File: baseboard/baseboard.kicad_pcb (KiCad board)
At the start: 2 copper layers, 99.8 x 99.8 mm, 36 parts, among them IC1 ATA6561-GAQW-N, J11 Conn_01x02_Pin, J13 Conn_02x05_Odd_Even, J14 Conn_02x25_Odd_Even, J6 Screw_Terminal_01x02, J7 Conn_02x25_Odd_Even, J8 Conn_01x02_Pin, U1 PY32E407V1xT_START

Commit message: artwork confirm
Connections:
- J14 pad 19: /WIPER -> /F2
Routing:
- net /Pmod3_2: track 43.6 -> 79.8 mm
- net /WIPER: track 8.44 -> 0.00 mm
- net /F2: track 0.00 -> 8.44 mm
- net /ETH_RMII_TXD1: track 26.5 -> 24.2 mm
- net /Pmod2_4: track 78.8 -> 80.9 mm
- net +3V3: track 423.5 -> 422.4 mm
- net /Pmod3_1: track 48.8 -> 49.5 mm
- net /Pmod2_3: track 43.5 -> 44.1 mm
- net GND: vias 84 -> 89
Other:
- board size 99.8 x 99.8 mm -> 99.8 x 93.2 mm
- board text added: "5V"
- board text added: "A3"
- board text added: "A4"
- board text added: "A5"
- board text added: "A6"
- board text added: "B12|B11"
- board text added: "B2|E13"
- board text added: "C10|A11"
- board text added: "C12|A10"
- board text added: "C6"
- board text added: "C7"
- board text added: "D10|D9"
- board text added: "D13"
- board text added: "D14"
- board text added: "D2|F4"
- board text added: "D3|D7"
- board text added: "D4|C9"
- board text added: "D5|B6"
- board text added: "D6|C8"
- board text added: "D8|A1"
- board text added: "E0|E5"
- board text added: "E15|D15"
- board text added: "E1|E6"
- board text added: "E2|E4"
- board text added: "E3|E14"
- board text added: "E7|E12"
- board text added: "E8|E11"
- board text added: "E9|E10"
- board text added: "G"
- board text added: "H L"
- board text added: "NC|A2"
- board text added: "NC|B13"
- board text added: "NC|C1"
- board text added: "NRST"
- board text added: "Pmod EXP v0.1 for PY32E407-START-ETH V2.1"
- board text added: "RXD"
- board text added: "TXD"
- board text added: "V"

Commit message: plot
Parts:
- moved J6 5.08 mm to (117.3, 83.7), turned to 180 degrees
- moved D5 0.25 mm to (114.8, 80.0)
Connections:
- D5 pad 1: Net-(J6-Pin_2) -> Net-(J6-Pin_1)
- J6 pad 1: Net-(J11-Pin_2) -> Net-(J6-Pin_1)
- J6 pad 2: Net-(J6-Pin_2) -> Net-(J11-Pin_2)
- J8 pad 1: Net-(J6-Pin_2) -> Net-(J6-Pin_1)
- L1 pad 2: Net-(J6-Pin_2) -> Net-(J6-Pin_1)
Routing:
- net Net-(J6-Pin_2): track 27.1 -> 0.00 mm
- net Net-(J6-Pin_1): track 0.00 -> 27.1 mm
- net +3V3: track 422.4 -> 434.1 mm
- net GND: track 40.4 -> 49.9 mm, vias 89 -> 92
- net Net-(J8-Pin_2): track 3.16 -> 2.65 mm
- net Net-(J11-Pin_1): track 3.15 -> 2.64 mm
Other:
- board text added: "3V3"
- board text added: "G|3V3"
- board text added: "JTCK"
- board text added: "JTDI"
- board text added: "JTDO"
- board text added: "JTMS"
- board text added: "NC"
- board text added: "VREF|VSSA"

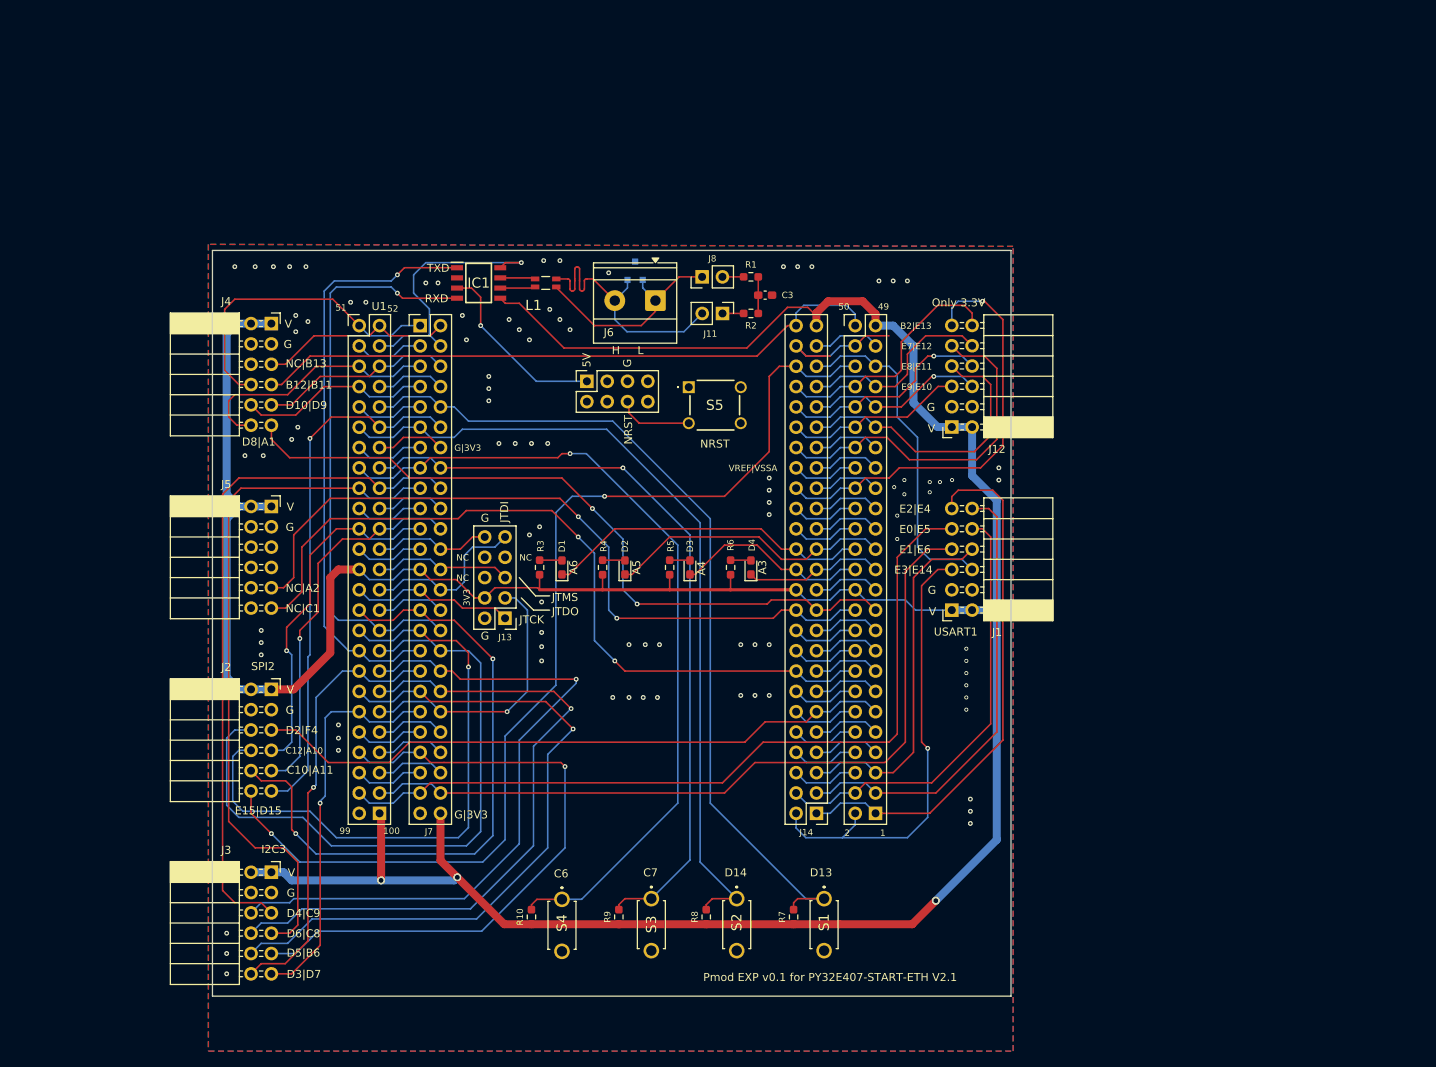
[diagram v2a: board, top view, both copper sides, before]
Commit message: add t1s on baseboard
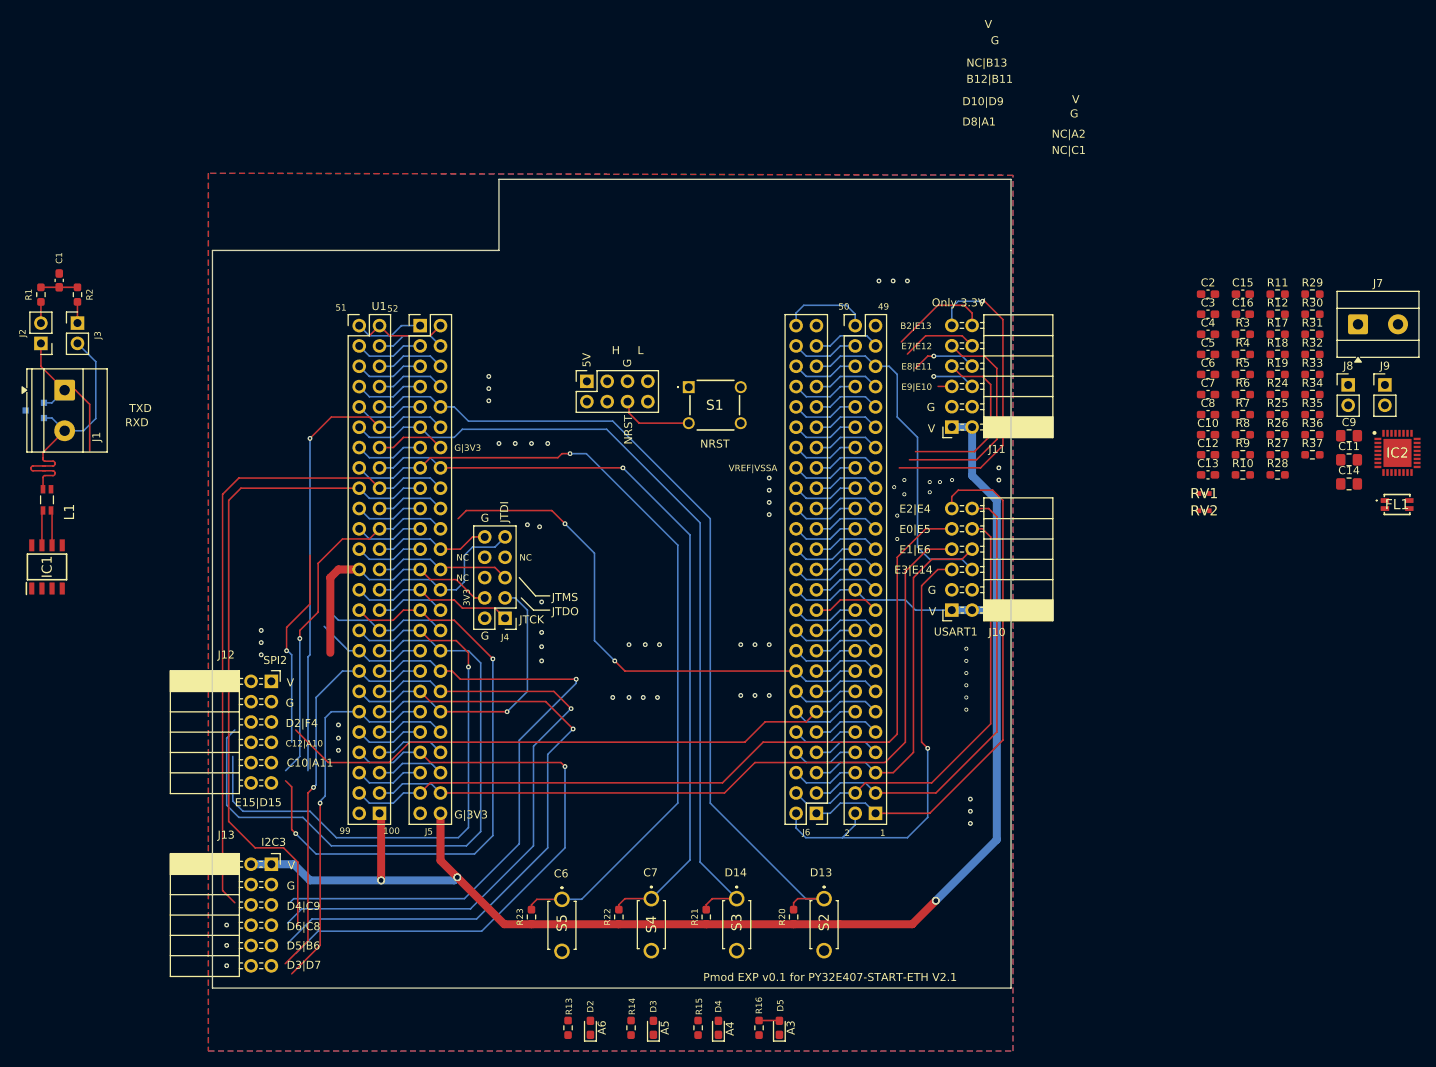
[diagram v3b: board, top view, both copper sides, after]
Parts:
- removed the J4 at (69.3, 86.6)
- removed the J5 at (69.3, 109.5)
- added C10: 0.1u, Capacitor_SMD:C_0603_1608Metric_Pad1.08x0.95mm_HandSolder, F.Cu at (186.4, 100.5)
- added C11: 10u, Capacitor_SMD:C_0805_2012Metric_Pad1.18x1.45mm_HandSolder, F.Cu at (204.1, 103.6)
- added C12: 10000p, Capacitor_SMD:C_0603_1608Metric_Pad1.08x0.95mm_HandSolder, F.Cu at (186.4, 103.0)
- added C13: 0.1u, Capacitor_SMD:C_0603_1608Metric_Pad1.08x0.95mm_HandSolder, F.Cu at (186.4, 105.5)
- added C14: 10u, Capacitor_SMD:C_0805_2012Metric_Pad1.18x1.45mm_HandSolder, F.Cu at (204.1, 106.7)
- added C15: 10000p, Capacitor_SMD:C_0603_1608Metric_Pad1.08x0.95mm_HandSolder, F.Cu at (190.8, 82.9)
- added C16: 0.1u, Capacitor_SMD:C_0603_1608Metric_Pad1.08x0.95mm_HandSolder, F.Cu at (190.8, 85.4)
- added C2: 0.22u, Capacitor_SMD:C_0603_1608Metric_Pad1.08x0.95mm_HandSolder, F.Cu at (186.4, 82.9)
- added C3: 0.22u, Capacitor_SMD:C_0603_1608Metric_Pad1.08x0.95mm_HandSolder, F.Cu at (186.4, 85.4)
- added C4: 0.1u, Capacitor_SMD:C_0603_1608Metric_Pad1.08x0.95mm_HandSolder, F.Cu at (186.4, 88.0)
- added C5: 0.1u, Capacitor_SMD:C_0603_1608Metric_Pad1.08x0.95mm_HandSolder, F.Cu at (186.4, 90.5)
- added C6: 10000p, Capacitor_SMD:C_0603_1608Metric_Pad1.08x0.95mm_HandSolder, F.Cu at (186.4, 93.0)
- added C7: 0.1u, Capacitor_SMD:C_0603_1608Metric_Pad1.08x0.95mm_HandSolder, F.Cu at (186.4, 95.5)
- added C8: 10000p, Capacitor_SMD:C_0603_1608Metric_Pad1.08x0.95mm_HandSolder, F.Cu at (186.4, 98.0)
- added C9: 10u, Capacitor_SMD:C_0805_2012Metric_Pad1.18x1.45mm_HandSolder, F.Cu at (204.1, 100.6)
- added FL1: ACT1210E-131-2P-TL00, kicad9_samacsys:ACT1210E1312PTL00, F.Cu at (210.1, 109.2)
- added IC2: LAN8670C2-E_LMX, kicad9_samacsys:QFN50P500X500X100-33N-D, F.Cu at (210.1, 102.8)
- added J7: Screw_Terminal_01x02, TerminalBlock_MetzConnect:TerminalBlock_MetzConnect_Type055_RT01502HDWU_1x02_P5.00mm_Horizontal, F.Cu at (205.2, 86.7)
- added J8: Conn_01x02_Pin, Connector_PinHeader_2.54mm:PinHeader_1x02_P2.54mm_Vertical, F.Cu at (203.9, 94.3)
- added J9: Conn_01x02_Pin, Connector_PinHeader_2.54mm:PinHeader_1x02_P2.54mm_Vertical, F.Cu at (208.5, 94.3)
- added R10: 10k, Resistor_SMD:R_0603_1608Metric_Pad0.98x0.95mm_HandSolder, F.Cu at (190.8, 105.5)
- added R11: 10k, Resistor_SMD:R_0603_1608Metric_Pad0.98x0.95mm_HandSolder, F.Cu at (195.1, 82.9)
- added R12: 10k, Resistor_SMD:R_0603_1608Metric_Pad0.98x0.95mm_HandSolder, F.Cu at (195.1, 85.4)
- added R17: 10k, Resistor_SMD:R_0603_1608Metric_Pad0.98x0.95mm_HandSolder, F.Cu at (195.1, 88.0)
- added R18: 10k, Resistor_SMD:R_0603_1608Metric_Pad0.98x0.95mm_HandSolder, F.Cu at (195.1, 90.5)
- added R19: 10k, Resistor_SMD:R_0603_1608Metric_Pad0.98x0.95mm_HandSolder, F.Cu at (195.1, 93.0)
- added R24: 4.7k, Resistor_SMD:R_0603_1608Metric_Pad0.98x0.95mm_HandSolder, F.Cu at (195.1, 95.5)
- added R25: 4.7k, Resistor_SMD:R_0603_1608Metric_Pad0.98x0.95mm_HandSolder, F.Cu at (195.1, 98.0)
- added R26: 22, Resistor_SMD:R_0603_1608Metric_Pad0.98x0.95mm_HandSolder, F.Cu at (195.1, 100.5)
- added R27: 12.4k, Resistor_SMD:R_0603_1608Metric_Pad0.98x0.95mm_HandSolder, F.Cu at (195.1, 103.0)
- added R28: 22, Resistor_SMD:R_0603_1608Metric_Pad0.98x0.95mm_HandSolder, F.Cu at (195.1, 105.5)
- added R29: 22, Resistor_SMD:R_0603_1608Metric_Pad0.98x0.95mm_HandSolder, F.Cu at (199.5, 82.9)
- added R3: 49.9, Resistor_SMD:R_0603_1608Metric_Pad0.98x0.95mm_HandSolder, F.Cu at (190.8, 88.0)
- added R30: 10k, Resistor_SMD:R_0603_1608Metric_Pad0.98x0.95mm_HandSolder, F.Cu at (199.5, 85.4)
- added R31: 10k, Resistor_SMD:R_0603_1608Metric_Pad0.98x0.95mm_HandSolder, F.Cu at (199.5, 88.0)
- added R32: 4.7k, Resistor_SMD:R_0603_1608Metric_Pad0.98x0.95mm_HandSolder, F.Cu at (199.5, 90.5)
- added R33: 10k, Resistor_SMD:R_0603_1608Metric_Pad0.98x0.95mm_HandSolder, F.Cu at (199.5, 93.0)
- added R34: 10k, Resistor_SMD:R_0603_1608Metric_Pad0.98x0.95mm_HandSolder, F.Cu at (199.5, 95.5)
- added R35: 10k, Resistor_SMD:R_0603_1608Metric_Pad0.98x0.95mm_HandSolder, F.Cu at (199.5, 98.0)
- added R36: 10k, Resistor_SMD:R_0603_1608Metric_Pad0.98x0.95mm_HandSolder, F.Cu at (199.5, 100.5)
- added R37: 10k, Resistor_SMD:R_0603_1608Metric_Pad0.98x0.95mm_HandSolder, F.Cu at (199.5, 103.0)
- added R4: 49.9, Resistor_SMD:R_0603_1608Metric_Pad0.98x0.95mm_HandSolder, F.Cu at (190.8, 90.5)
- added R5: 10k, Resistor_SMD:R_0603_1608Metric_Pad0.98x0.95mm_HandSolder, F.Cu at (190.8, 93.0)
- added R6: 10k, Resistor_SMD:R_0603_1608Metric_Pad0.98x0.95mm_HandSolder, F.Cu at (190.8, 95.5)
- added R7: 10k, Resistor_SMD:R_0603_1608Metric_Pad0.98x0.95mm_HandSolder, F.Cu at (190.8, 98.0)
- added R8: 10k, Resistor_SMD:R_0603_1608Metric_Pad0.98x0.95mm_HandSolder, F.Cu at (190.8, 100.5)
- added R9: 10k, Resistor_SMD:R_0603_1608Metric_Pad0.98x0.95mm_HandSolder, F.Cu at (190.8, 103.0)
- added RV1: AVRH10C221KT1R5YA8, kicad9_samacsys:RESC1005X55N, F.Cu at (185.9, 107.9)
- added RV2: AVRH10C221KT1R5YA8, kicad9_samacsys:RESC1005X55N, F.Cu at (185.9, 110.0)
- moved R1 88.8 mm to (40.5, 83.0), turned to -90 degrees
- moved C1 88.3 mm to (42.8, 81.2), turned to 90 degrees
- moved R2 84.2 mm to (45.1, 83.0), turned to 90 degrees
- moved J2 83.1 mm to (40.5, 89.1), turned to 180 degrees
- moved J3 80.6 mm to (45.1, 86.5), turned to 0 degrees
- moved D1 77.0 mm to (39.8, 97.5), turned to -90 degrees
- moved J1 74.7 mm to (43.5, 94.9), turned to -90 degrees
- moved L1 68.0 mm to (41.3, 108.6), turned to 90 degrees
- moved IC1 64.6 mm to (41.3, 117.0), turned to 90 degrees
- moved D2 57.7 mm to (109.2, 174.6)
- moved D3 57.7 mm to (117.1, 174.6)
- moved D4 57.7 mm to (125.2, 174.6)
- moved D5 57.7 mm to (132.8, 174.6)
- moved R13 57.7 mm to (106.4, 174.6)
- moved R14 57.7 mm to (114.3, 174.6)
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- renumbered C3 to C1, D5 to D1, D1 to D2, D2 to D3, D3 to D4, D4 to D5, J6 to J1, J1 to J10, J12 to J11, J2 to J12, J3 to J13, J8 to J2, J11 to J3, J13 to J4, J7 to J5, J14 to J6, R3 to R13, R4 to R14, R5 to R15, R6 to R16, R7 to R20, R8 to R21, R9 to R22, R10 to R23, S5 to S1, S1 to S2, S2 to S3, S3 to S4, S4 to S5
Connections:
- J6 pad 1: /Pmod1_1 -> /Pmod1_4
- J6 pad 10: /F3 -> /C15
- J6 pad 11: /Pmod2_4 -> /F0
- J6 pad 12: /F0 -> /Pmod2_4
- J6 pad 13: /F1 -> /F5
- J6 pad 14: /F5 -> /F1
- J6 pad 15: /C0 -> /ETH_MDC
- J6 pad 16: /ETH_MDC -> /C0
- J6 pad 17: /C2 -> /C3
- J6 pad 18: /C3 -> /C2
- J6 pad 19: /F2 -> /A0
- J6 pad 2: /Pmod1_4 -> /Pmod1_1
- J6 pad 20: /A0 -> /F2
- J6 pad 21: /ETH_RMII_REF_CLK -> /ETH_MDIO
- J6 pad 22: /ETH_MDIO -> /CLK50M
- J6 pad 23: GND -> +3V3
- J6 pad 24: +3V3 -> GND
- J6 pad 25: /A3 -> /A4
- J6 pad 26: /A4 -> /A3
- J6 pad 27: /A5 -> /A6
- J6 pad 28: /A6 -> /A5
- J6 pad 29: /A7 -> /C4
- J6 pad 3: /Pmod1_5 -> /Pmod1_6
- J6 pad 30: /C4 -> /A7
- J6 pad 31: /C5 -> /B0
- J6 pad 32: /B0 -> /C5
- J6 pad 33: /B1 -> /Pmod4_1
- J6 pad 34: /Pmod4_1 -> /B1
- J6 pad 35: /VSSA -> /VREF+
- J6 pad 36: /VREF+ -> /VSSA
- J6 pad 37: /VCCA -> /Pmod4_2
- J6 pad 38: /Pmod4_2 -> /VCCA
- J6 pad 39: /Pmod4_3 -> /Pmod4_4
- J6 pad 4: /Pmod1_6 -> /Pmod1_5
- J6 pad 40: /Pmod4_4 -> /Pmod4_3
- J6 pad 41: /Pmod4_5 -> /Pmod4_6
- J6 pad 42: /Pmod4_6 -> /Pmod4_5
- J6 pad 43: /Pmod4_7 -> /Pmod4_8
- J6 pad 44: /Pmod4_8 -> /Pmod4_7
- J6 pad 45: /Pmod1_8 -> /Pmod2_5
- J6 pad 46: /Pmod2_5 -> /Pmod1_8
- J6 pad 47: /B10 -> GND
- J6 pad 48: GND -> /B10
- J6 pad 49: +3V3 -> /ETH_RMII_TX_EN
- J6 pad 5: /Pmod1_7 -> /VBAT
- J6 pad 50: /ETH_RMII_TX_EN -> +3V3
- J6 pad 6: /VBAT -> /Pmod1_7
- J6 pad 7: /C13 -> /C14
- J6 pad 8: /C14 -> /C13
- J6 pad 9: /C15 -> /F3
- U1 pad 1: /Pmod1_1 -> /Pmod1_4
- U1 pad 10: /F3 -> /C15
- U1 pad 11: /Pmod2_4 -> /F0
- U1 pad 12: /F0 -> /Pmod2_4
- U1 pad 13: /F1 -> /F5
- U1 pad 14: /F5 -> /F1
- U1 pad 15: /C0 -> /ETH_MDC
- U1 pad 16: /ETH_MDC -> /C0
- U1 pad 17: /C2 -> /C3
- U1 pad 18: /C3 -> /C2
- U1 pad 19: /F2 -> /A0
- U1 pad 2: /Pmod1_4 -> /Pmod1_1
- U1 pad 20: /A0 -> /F2
- U1 pad 21: /ETH_RMII_REF_CLK -> /ETH_MDIO
- U1 pad 22: /ETH_MDIO -> /CLK50M
- U1 pad 23: GND -> +3V3
- U1 pad 24: +3V3 -> GND
- U1 pad 25: /A3 -> /A4
- U1 pad 26: /A4 -> /A3
- U1 pad 27: /A5 -> /A6
- U1 pad 28: /A6 -> /A5
- U1 pad 29: /A7 -> /C4
- U1 pad 3: /Pmod1_5 -> /Pmod1_6
- U1 pad 30: /C4 -> /A7
- U1 pad 31: /C5 -> /B0
- U1 pad 32: /B0 -> /C5
- U1 pad 33: /B1 -> /Pmod4_1
- U1 pad 34: /Pmod4_1 -> /B1
- U1 pad 35: /VSSA -> /VREF+
- U1 pad 36: /VREF+ -> /VSSA
- U1 pad 37: /VCCA -> /Pmod4_2
- U1 pad 38: /Pmod4_2 -> /VCCA
- U1 pad 39: /Pmod4_3 -> /Pmod4_4
- U1 pad 4: /Pmod1_6 -> /Pmod1_5
- U1 pad 40: /Pmod4_4 -> /Pmod4_3
- U1 pad 41: /Pmod4_5 -> /Pmod4_6
- U1 pad 42: /Pmod4_6 -> /Pmod4_5
- U1 pad 43: /Pmod4_7 -> /Pmod4_8
- U1 pad 44: /Pmod4_8 -> /Pmod4_7
- U1 pad 45: /Pmod1_8 -> /Pmod2_5
- U1 pad 46: /Pmod2_5 -> /Pmod1_8
- U1 pad 47: /B10 -> GND
- U1 pad 48: GND -> /B10
- U1 pad 49: +3V3 -> /ETH_RMII_TX_EN
- U1 pad 5: /Pmod1_7 -> /VBAT
- U1 pad 50: /ETH_RMII_TX_EN -> +3V3
- U1 pad 6: /VBAT -> /Pmod1_7
- U1 pad 7: /C13 -> /C14
- U1 pad 8: /C14 -> /C13
- U1 pad 9: /C15 -> /F3
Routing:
- net +3V3: track 434.1 -> 260.8 mm
- net /Pmod2_5: track 133.3 -> 0.00 mm, vias 2 -> 0
- net /ETH_RMII_REF_CLK: track 91.3 -> 0.00 mm, vias 2 -> 0
- net /ETH_MDC: track 97.1 -> 8.44 mm, vias 2 -> 0
- net /ETH_MDIO: track 93.0 -> 8.44 mm, vias 2 -> 0
- net /ETH_RMII_TX_EN: track 79.9 -> 0.00 mm
- net /Pmod2_4: track 80.9 -> 8.44 mm
- net /F0: track 8.44 -> 77.8 mm
- net /CAN_TXD: track 74.0 -> 14.3 mm, vias 1 -> 0
- net /C0: track 8.44 -> 65.8 mm, vias 0 -> 2
- net /CAN_RXD: track 72.4 -> 15.8 mm, vias 1 -> 0
- net /A6: track 41.1 -> 8.44 mm
- net /ETH_RMII_TXD0: track 39.0 -> 8.67 mm
- net /A5: track 36.0 -> 8.44 mm
- net /B15: track 34.2 -> 8.67 mm, vias 1 -> 0
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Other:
- board size 99.8 x 93.2 mm -> 99.8 x 101.1 mm

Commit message: schematics
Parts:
- moved IC2 90.1 mm to (124.7, 74.2), turned to 90 degrees
- moved J9 74.9 mm to (142.7, 58.4)
- moved FL1 74.2 mm to (143.8, 75.9)
- moved J8 63.3 mm to (149.9, 61.5)
- moved RV1 53.5 mm to (148.6, 69.6)
- moved J7 51.8 mm to (155.2, 73.2), turned to -90 degrees
- moved RV2 48.4 mm to (147.0, 81.3)
- moved D2 25.8 mm to (101.6, 150.0)
- moved R13 25.8 mm to (98.8, 150.0)
- moved S1 25.5 mm to (96.1, 92.5)
- moved R14 25.4 mm to (108.2, 150.0)
- moved D3 25.4 mm to (111.0, 150.0)
- moved D4 25.1 mm to (120.1, 150.0)
- moved R15 25.1 mm to (117.6, 150.0)
- moved D5 25.0 mm to (128.8, 150.0)
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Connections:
- J6 pad 10: /C15 -> unconnected-(J6-Pin_9-Pad10)
- J6 pad 7: /C14 -> unconnected-(J6-Pin_8-Pad7)
- R20 pad 2: /D13 -> /F3
- R21 pad 2: /D14 -> /C13
- R22 pad 2: /C7 -> /B7
- R23 pad 2: /C6 -> /B9
- S2 pad 1: /D13 -> /F3
- S3 pad 1: /D14 -> /C13
- S4 pad 1: /C7 -> /B7
- S5 pad 1: /C6 -> /B9
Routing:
- net /D13: track 107.8 -> 8.67 mm
- net /D14: track 103.1 -> 8.67 mm
- net /C6: track 102.8 -> 8.67 mm, vias 1 -> 0
- net /C7: track 95.8 -> 8.67 mm, vias 1 -> 0
- net /F0: track 77.8 -> 8.44 mm
- net /C0: track 65.8 -> 8.44 mm, vias 2 -> 0
- net /B7: track 8.67 -> 52.8 mm, vias 0 -> 1
- net /B9: track 8.57 -> 47.2 mm, vias 0 -> 1
- net /C13: track 8.44 -> 36.5 mm
- net +3V3: track 260.8 -> 239.2 mm
- net /Pmod1_2: track 101.7 -> 120.8 mm
- net /Pmod1_3: track 97.6 -> 116.0 mm
- net /Pmod1_8: track 50.6 -> 33.7 mm
- net /Pmod1_4: track 57.4 -> 42.3 mm
- net /Pmod1_7: track 53.3 -> 39.1 mm
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
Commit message: base baord schematics
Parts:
- added R38: 22, Resistor_SMD:R_0603_1608Metric_Pad0.98x0.95mm_HandSolder, F.Cu at (126.3, 117.9)
- added R39: 22, Resistor_SMD:R_0603_1608Metric_Pad0.98x0.95mm_HandSolder, F.Cu at (126.3, 120.4)
- added Y1: CB3LV-3C-50M0000, kicad9_samacsys:CB3LV3C50M0000, F.Cu at (119.4, 107.6)
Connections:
- J6 pad 22: /CLK50M -> /ETH_RMII_REF_CLK
- U1 pad 22: /CLK50M -> /ETH_RMII_REF_CLK
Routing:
- net /Pmod4_1: track 48.2 -> 8.44 mm, vias 1 -> 0
- net /Pmod4_2: track 36.1 -> 8.44 mm
- net /Pmod4_7: track 18.0 -> 40.8 mm
- net /Pmod4_3: track 30.9 -> 43.7 mm
- net /Pmod4_5: track 14.0 -> 25.1 mm, vias 1 -> 0
- net /Pmod4_8: track 21.1 -> 31.8 mm
- net /ETH_RMII_REF_CLK: track 0.00 -> 8.44 mm
- net /CLK50M: track 8.44 -> 0.00 mm
- net /Pmod4_6: track 16.7 -> 8.44 mm, vias 1 -> 0
- net /Pmod4_4: track 10.2 -> 8.44 mm

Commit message: base board schematics
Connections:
- J11 pad 10: /Pmod4_5 -> /Pmod4_8
- J11 pad 7: /Pmod4_8 -> /Pmod4_5
- J11 pad 8: /Pmod4_7 -> /Pmod4_6
- J11 pad 9: /Pmod4_6 -> /Pmod4_7
- J6 pad 33: /Pmod4_1 -> /Pmod4_7
- J6 pad 37: /Pmod4_2 -> /Pmod4_8
- J6 pad 4: /Pmod1_5 -> /Pmod1_8
- J6 pad 42: /Pmod4_5 -> /Pmod4_2
- J6 pad 43: /Pmod4_8 -> /Pmod4_5
- J6 pad 44: /Pmod4_7 -> /Pmod4_1
- J6 pad 46: /Pmod1_8 -> /Pmod1_5
- U1 pad 33: /Pmod4_1 -> /Pmod4_7
- U1 pad 37: /Pmod4_2 -> /Pmod4_8
- U1 pad 4: /Pmod1_5 -> /Pmod1_8
- U1 pad 42: /Pmod4_5 -> /Pmod4_2
- U1 pad 43: /Pmod4_8 -> /Pmod4_5
- U1 pad 44: /Pmod4_7 -> /Pmod4_1
- U1 pad 46: /Pmod1_8 -> /Pmod1_5
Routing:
- net /F3: track 15.6 -> 58.1 mm
- net /Pmod1_5: track 49.6 -> 8.44 mm
- net /Pmod1_2: track 120.8 -> 100.3 mm
- net /Pmod4_3: track 43.7 -> 23.7 mm
- net /Pmod1_3: track 116.0 -> 96.3 mm
- net /Pmod4_1: track 8.44 -> 23.7 mm
- net /Pmod4_6: track 8.44 -> 23.7 mm
- net /Pmod4_2: track 8.44 -> 23.7 mm
- net /Pmod1_1: track 63.5 -> 76.8 mm
- net /Pmod1_8: track 33.7 -> 45.6 mm
- net /Pmod4_4: track 8.44 -> 20.1 mm
- net /Pmod1_6: track 45.0 -> 52.5 mm
- net /Pmod1_7: track 39.1 -> 46.2 mm
- net /Pmod1_4: track 42.3 -> 44.9 mm
- net /Pmod4_7: track 40.8 -> 38.3 mm
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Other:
- board text added: "E10|E11"
- board text added: "E12|E13"
- board text added: "E8|B2"
- board text added: "E9|E7"
- board text removed: "B2|E13"
- board text removed: "E7|E12"
- board text removed: "E8|E11"
- board text removed: "E9|E10"

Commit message: base board schematics
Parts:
- Y1: footprint kicad9_samacsys:CB3LV3C50M0000 -> samacsys:CB3LV3C50M0000
- moved R23 5.62 mm to (102.5, 155.2), turned to 0 degrees
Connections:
- J5 pad 36: /Pmod3_8 -> /Pmod3_6
- J5 pad 37: /Pmod3_6 -> /Pmod3_7
- J5 pad 38: /Pmod3_7 -> /Pmod3_8
- J5 pad 41: /B4 -> /Pmod2_5
- J6 pad 45: /Pmod2_5 -> /E15
- U1 pad 45: /Pmod2_5 -> /E15
- U1 pad 86: /Pmod3_8 -> /Pmod3_6
- U1 pad 87: /Pmod3_6 -> /Pmod3_7
- U1 pad 88: /Pmod3_7 -> /Pmod3_8
- U1 pad 91: /B4 -> /Pmod2_5
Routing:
- net /Pmod2_8: track 79.8 -> 8.67 mm
- net /Pmod2_6: track 76.1 -> 8.67 mm, vias 2 -> 0
- net /Pmod2_7: track 75.2 -> 8.67 mm, vias 1 -> 0
- net /C8: track 84.4 -> 112.8 mm, vias 0 -> 1
- net /Pmod3_5: track 50.3 -> 77.7 mm, vias 1 -> 0
- net /Pmod3_2: track 76.8 -> 53.0 mm
- net /C9: track 81.3 -> 104.5 mm, vias 0 -> 1
- net /Pmod2_5: track 8.44 -> 31.1 mm
- net /Pmod3_8: track 81.3 -> 63.4 mm, vias 1 -> 0
- net /A11: track 43.2 -> 28.5 mm, vias 1 -> 0
- net /Pmod3_1: track 47.0 -> 60.8 mm
- net /Pmod3_6: track 83.4 -> 70.7 mm, vias 1 -> 0
- net /Pmod2_3: track 33.6 -> 21.8 mm, vias 1 -> 0
- net /Pmod3_7: track 79.7 -> 69.8 mm, vias 1 -> 0
- net /B4: track 8.67 -> 0.00 mm
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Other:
- board text added: "B4|D15"
- board text added: "D|B"
- board text added: "D|C"
- board text added: "D|D"
- board text removed: "D3|D7"
- board text removed: "D4|C9"
- board text removed: "D5|B6"
- board text removed: "D6|C8"
- board text removed: "E15|D15"

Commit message: base board schematics
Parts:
- added C17: 0.1u, Capacitor_SMD:C_0603_1608Metric_Pad1.08x0.95mm_HandSolder, F.Cu at (74.2, 114.9)
- added C18: 0.1u, Capacitor_SMD:C_0603_1608Metric_Pad1.08x0.95mm_HandSolder, F.Cu at (66.0, 121.2)
- Y1: footprint samacsys:CB3LV3C50M0000 -> kicad9_samacsys:CB3LV3C50M0000
- moved R1 43.0 mm to (75.7, 107.7), turned to 90 degrees
- moved C1 38.2 mm to (64.3, 112.8), turned to -90 degrees
- moved J2 34.9 mm to (72.4, 103.4), turned to 90 degrees
- moved D1 32.6 mm to (72.0, 92.7), turned to 90 degrees
- moved R2 31.3 mm to (64.3, 107.7), turned to -90 degrees
- moved IC1 28.7 mm to (70.0, 118.5)
- moved L1 28.7 mm to (70.0, 110.1)
- moved J3 26.3 mm to (65.3, 103.4), turned to 90 degrees
- moved J1 24.4 mm to (67.4, 90.2)
- moved S1 12.8 mm to (105.7, 100.9)
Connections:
- D1 pad 1: Net-(J1-Pin_1) -> Net-(J1-Pin_2)
- D1 pad 2: Net-(J1-Pin_2) -> Net-(J1-Pin_1)
- J12 pad 2: /A11 -> /Pmod2_2
- J5 pad 21: /Pmod2_3 -> /Pmod2_2
- J5 pad 22: /A11 -> /Pmod2_3
- J5 pad 31: /Pmod2_7 -> /Pmod2_8
- J5 pad 34: /Pmod2_8 -> /Pmod2_7
- U1 pad 71: /Pmod2_3 -> /Pmod2_2
- U1 pad 72: /A11 -> /Pmod2_3
- U1 pad 81: /Pmod2_7 -> /Pmod2_8
- U1 pad 84: /Pmod2_8 -> /Pmod2_7
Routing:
- net /Pmod2_4: track 8.44 -> 147.0 mm
- net +5V: track 0.00 -> 68.8 mm, vias 0 -> 1
- net +3V3: track 234.5 -> 292.1 mm
- net /Pmod2_2: track 0.00 -> 54.6 mm
- net /Pmod2_6: track 8.67 -> 56.6 mm
- net /B15: track 8.67 -> 52.2 mm, vias 0 -> 1
- net /Pmod2_3: track 21.8 -> 53.2 mm
- net /A11: track 28.5 -> 0.00 mm
- net /Pmod2_1: track 65.3 -> 90.0 mm, vias 1 -> 0
- net /Pmod2_7: track 8.67 -> 31.0 mm
- net /Pmod2_8: track 8.67 -> 29.3 mm
- net /CAN_TXD: track 10.0 -> 25.6 mm
- net Net-(C1-Pad1): track 4.57 -> 14.6 mm, vias 0 -> 2
- net Net-(J1-Pin_2): track 34.8 -> 25.6 mm
- net /CAN_RXD: track 14.3 -> 21.2 mm
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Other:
- board size 99.8 x 101.1 mm -> 99.8 x 102.1 mm
